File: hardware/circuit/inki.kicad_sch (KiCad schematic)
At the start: 40 parts, among them J1 connector epaper, J2 Conn_01x02_Socket, J3 Conn_01x02_Socket, J4 Conn_01x02_Socket, J5 Conn_01x02_Socket, J7 Conn_01x02_Socket, Q1 TSM260P02CX, Q2 MMBT3904, Q3 IRLML6344TRPBF, SW1 SW_DIP_x04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

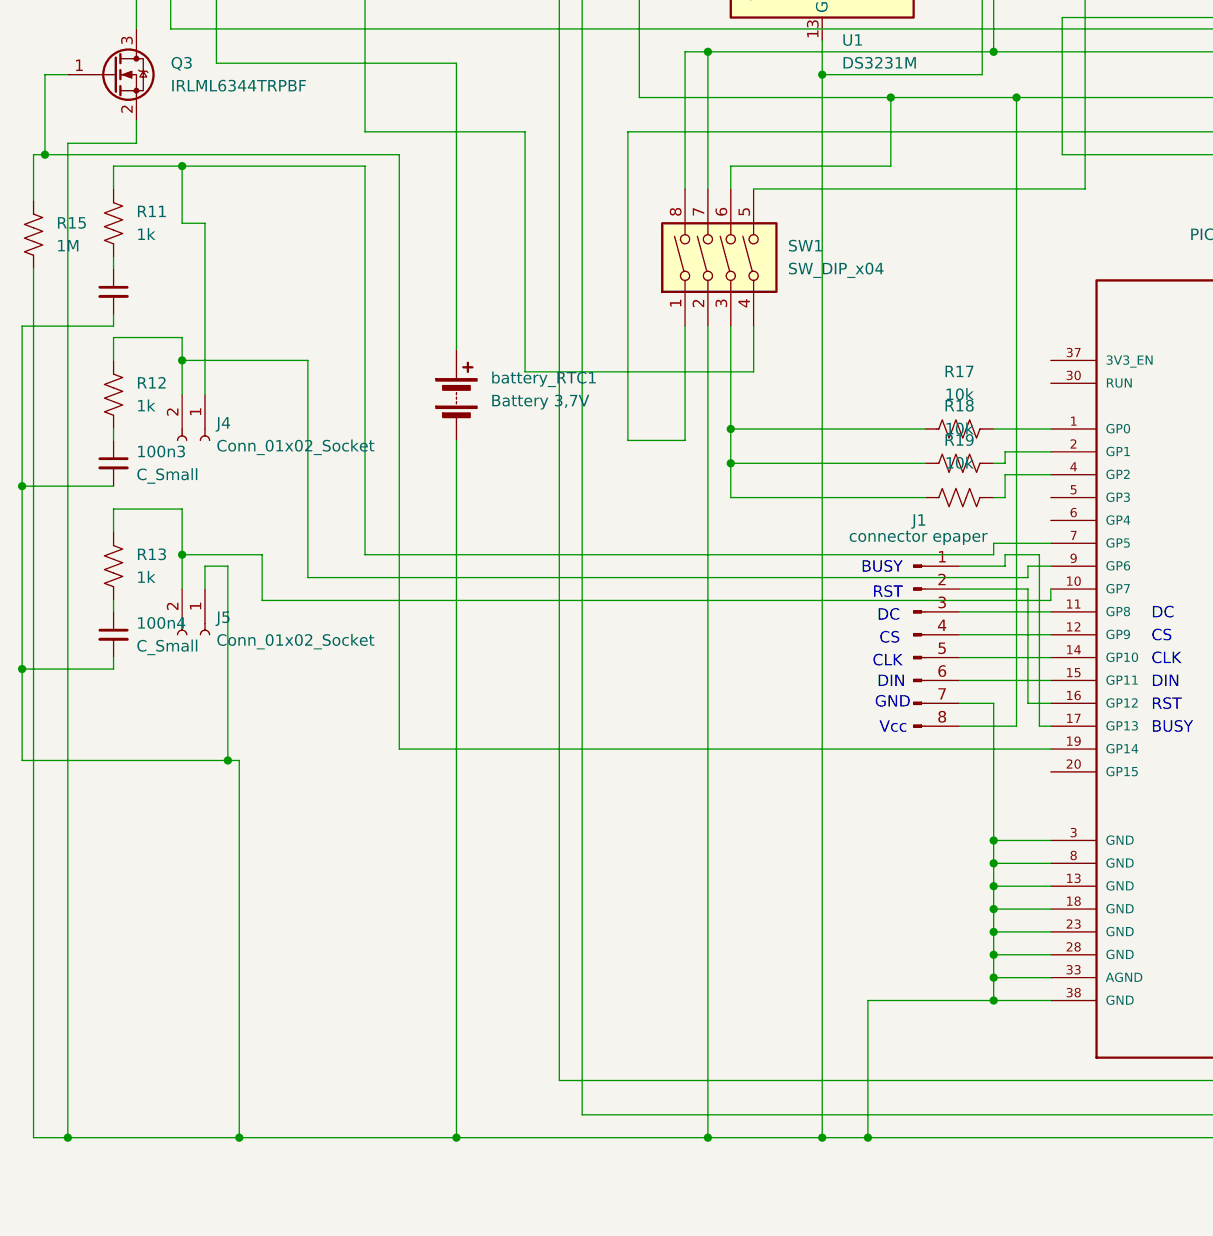
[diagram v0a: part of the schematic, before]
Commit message: modified pcb (all smds to one side), weathermap work
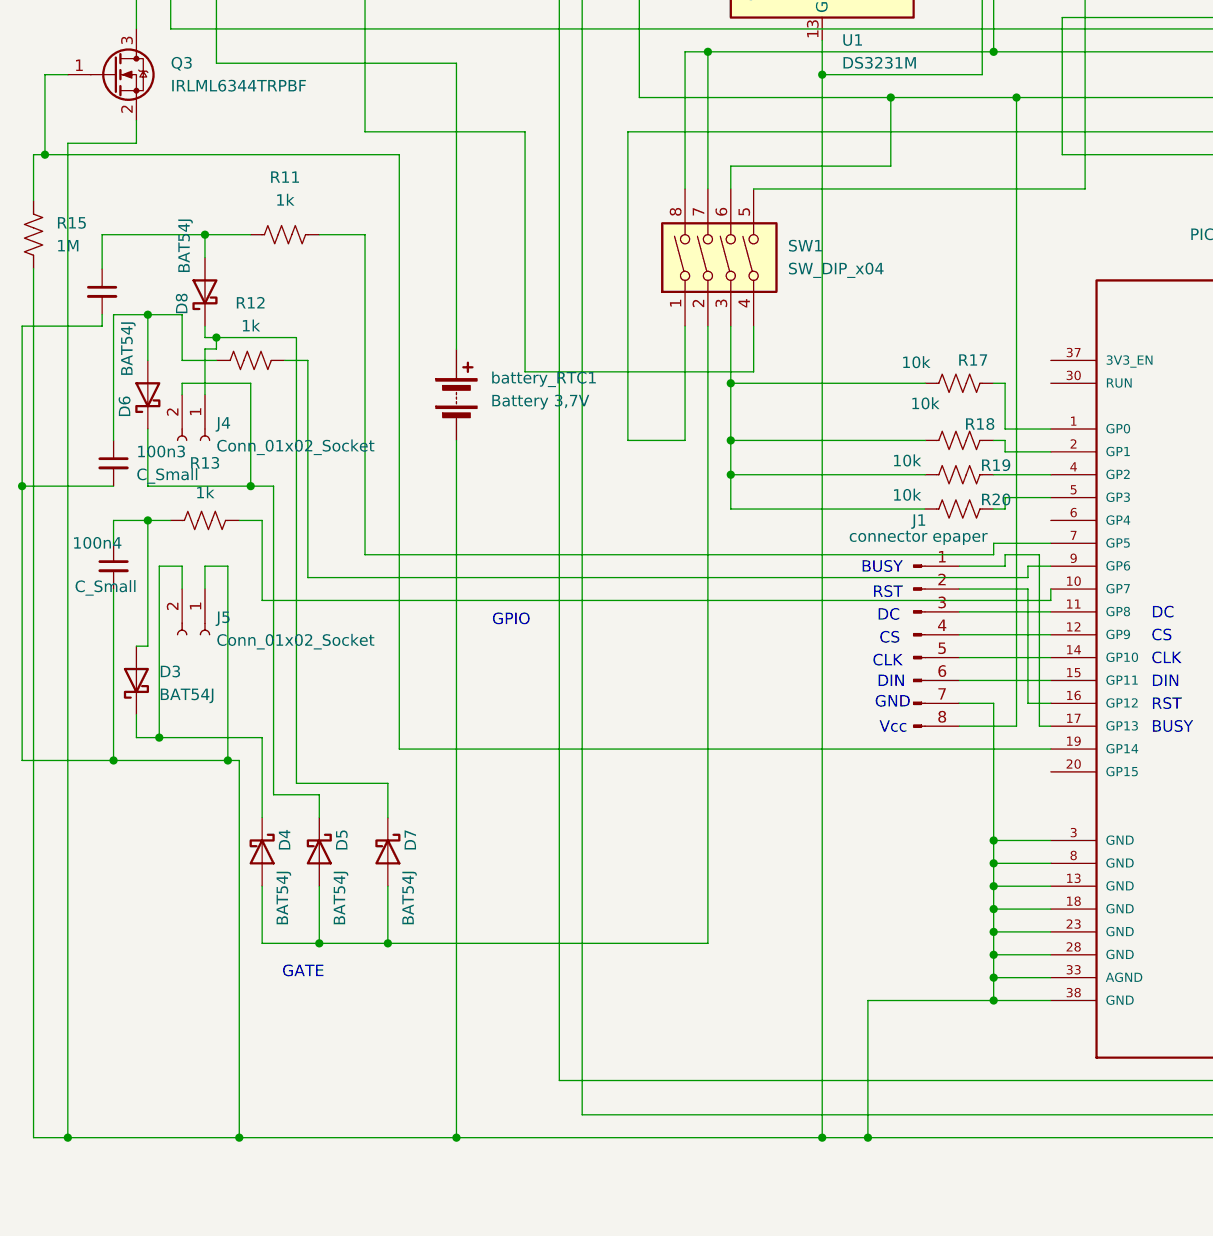
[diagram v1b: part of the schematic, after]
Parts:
- added D3, D4, D5, D6, D7, D8: BAT54J, Diode_SMD:D_SOD-323_HandSoldering, symbol Diode:BAT54J
- added R20: 10k, Resistor_SMD:R_0805_2012Metric_Pad1.20x1.40mm_HandSolder, symbol Device:R_US
- D1: footprint Diode_SMD:D_SOD-323F -> Diode_SMD:D_SOD-323_HandSoldering
- D2: footprint Diode_SMD:D_SOD-323 -> Diode_SMD:D_SOD-323_HandSoldering
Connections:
- net GND: no longer SW1.2
- net at R17.1, R18.1, R19.1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: now also R20.1
- net at R12.1: now also pico1.9 (GP6); no longer 100n3.1
- net at 100n4.1: now also R13.2, D3.2 (A); no longer R13.1
- net at pico1.5 (GP3): now also R20.2
- net at R11.1: now also pico1.7 (GP5); no longer 100n2.1
- new net: D3.1 (K), D4.1 (K), J5.2 (Pin_2)
- new net: D4.2 (A), D5.2 (A), D7.2 (A), SW1.2
- new net: 100n3.1, D6.2 (A), R12.2
- new net: R13.1, pico1.10 (GP7)
- new net: D7.1 (K), D8.1 (K), J4.1 (Pin_1)
- new net: D5.1 (K), D6.1 (K), J4.2 (Pin_2)
- new net: 100n2.1, D8.2 (A), R11.2
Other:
- note added: "GATE"
- note added: "GPIO"
- moved on the sheet: 100n4, R11, R12, R13, R17, R18, R19

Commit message: edit pcb: add bmp581
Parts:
- added U2: BMP581, symbol BMP581:BMP581
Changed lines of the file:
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@@
+	)
+	(symbol
+		(lib_id "BMP581:BMP581")
+		(at 250.19 148.59 0)
+		(unit 1)
+		(exclude_from_sim no)
+		(in_bom yes)
+		(on_board yes)
+		(dnp no)
+		(fields_autoplaced yes)
+		(property "Reference" "U2"
+			(at 250.825 138.43 0)
+			(effects
+				(font
+					(size 1.27 1.27)
+				)
+			)
+		)
+		(property "Value" "BMP581"
+			(at 250.825 140.97 0)
+			(effects
+				(font
+					(size 1.27 1.27)
+				)
+			)
+		)
+		(property "Footprint" ""
+			(at 250.19 148.59 0)
+			(effects
+				(font
+					(size 1.27 1.27)
+				)
+				(hide yes)
+			)
+		)
+		(property "Datasheet" ""
+			(at 250.19 148.59 0)
+			(effects
+				(font
+					(size 1.27 1.27)
+				)
+				(hide yes)
+			)
+		)
+		(property "Description" ""
+			(at 250.19 148.59 0)
+			(effects
+				(font
+					(size 1.27 1.27)
+				)
+				(hide yes)
+			)
+		)
+		(pin "8"
+		)
+		(pin "7"
+		)
+		(pin "4"
+		)
+		(pin "3"
+		)
+		(pin "1"
+		)
+		(pin "2"
+		)
+		(pin "6"
+		)
+		(pin "5"
+		)
+		(pin "10"
+		)
+		(pin "9"
+		)
+		(instances
+			(project ""
+				(path "/240a819b-80d5-474c-958b-cef4297f8f8c"
+					(reference "U2")
+					(unit 1)
+				)
+			)
+		)
 	)
 	(symbol

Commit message: default config weathermap
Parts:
- added 100n5: C_Small, Capacitor_SMD:C_0805_2012Metric, symbol Device:C_Small
- U2: footprint (none) -> inki:BMP581
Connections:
- net GND: now also U2.3 (VSS), U2.7 (INT), U2.8 (VSS), U2.9 (VSS), 100n5.2
- net at R3.2, U1.15 (SDA), pico1.26 (GP20): now also U2.4 (SDI)
- net at R4.2, U1.16 (SCL), pico1.27 (GP21): now also U2.2 (SCK)
- net at C1.1, C3.1, J1.8 (Pin_8)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: now also U2.1 (VDDIO), U2.10 (VDD), U2.5 (SDO), U2.6 (CSB), 100n5.1

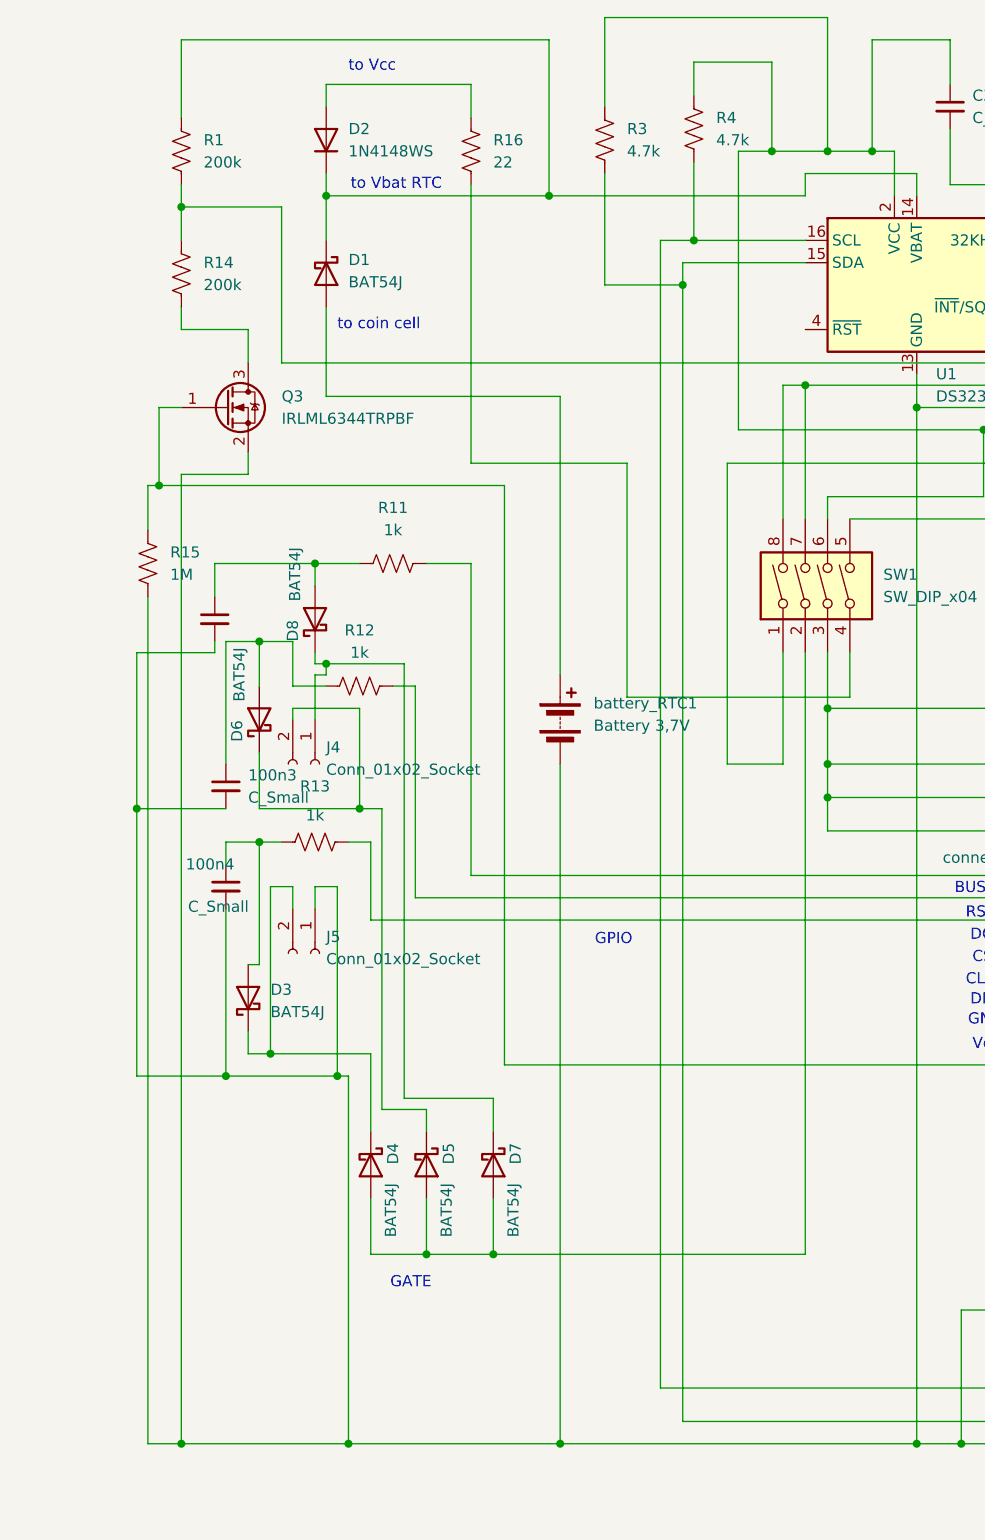
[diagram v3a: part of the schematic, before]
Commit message: hardware: gate VBAT divider with PFET to stop leakage in off-state
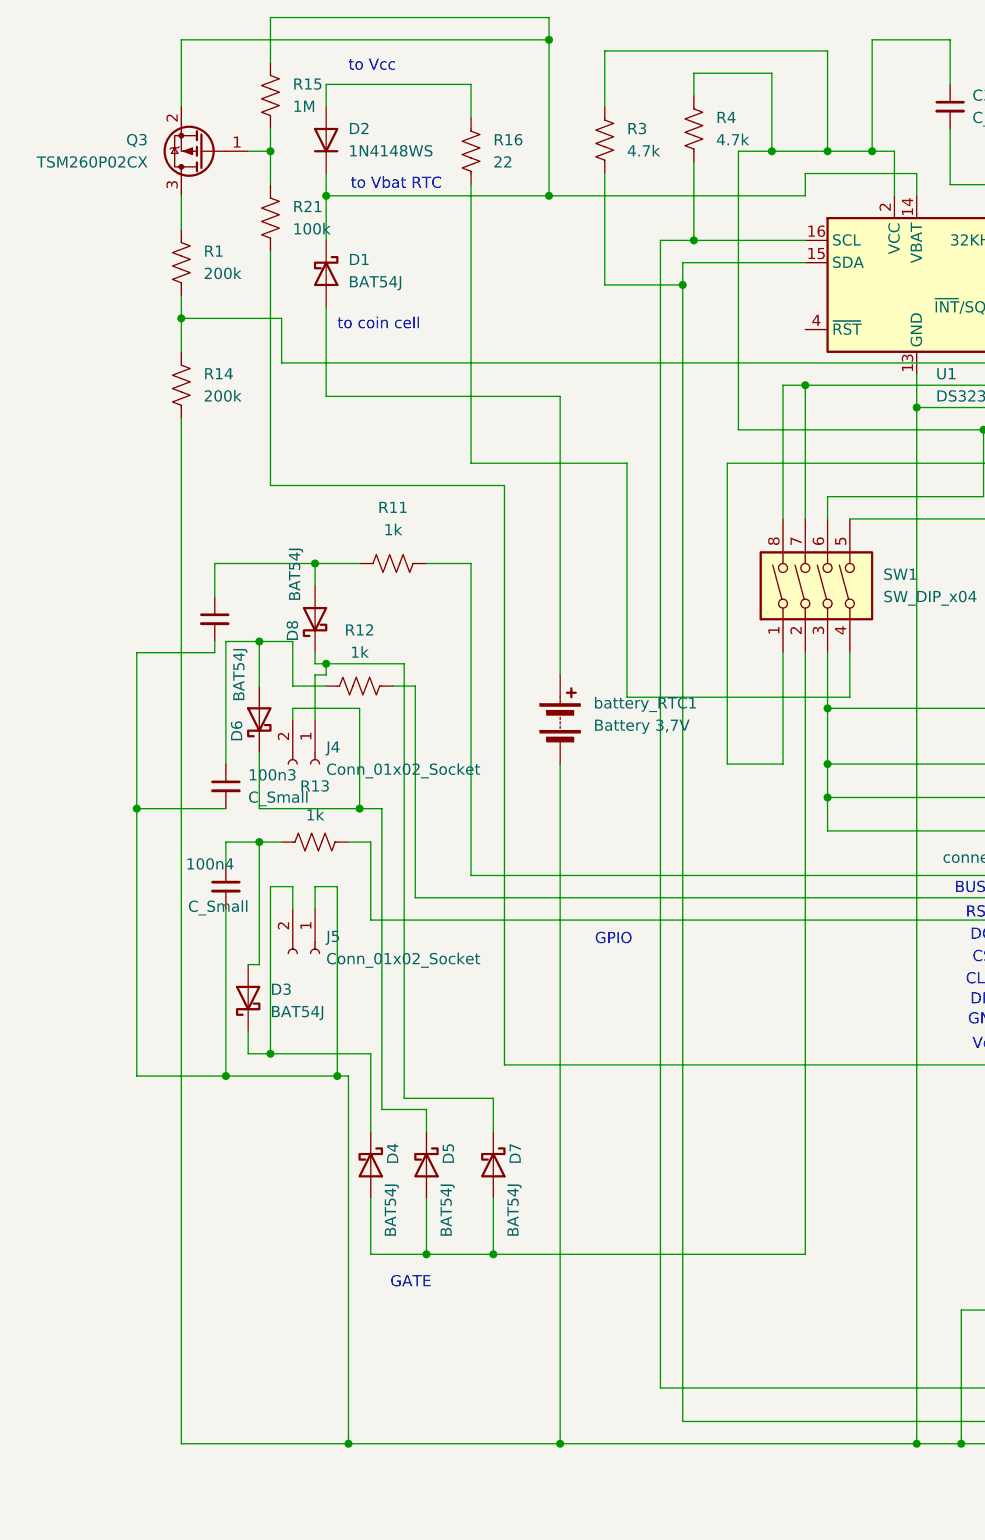
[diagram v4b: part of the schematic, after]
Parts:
- removed Q3: IRLML6344TRPBF, Package_TO_SOT_SMD:SOT-23, symbol Transistor_FET:IRLML0030
- added Q3: TSM260P02CX, Package_TO_SOT_SMD:SOT-23_Handsoldering, symbol Transistor_FET:TSM2301ACX
- added R21: 100k, Resistor_SMD:R_0805_2012Metric_Pad1.20x1.40mm_HandSolder, symbol Device:R_US
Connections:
- net GND: now also R14.2; no longer R15.2
- net at D1.1 (K), D2.1 (K), U1.14 (VBAT): now also R15.1, Q3.2 (S); no longer R1.1
- net at pico1.19 (GP14): now also R21.2; no longer R15.1
- new net: Q3.1 (G), R15.2, R21.1
- new net: Q3.3 (D), R1.1
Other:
- moved on the sheet: R1, R14

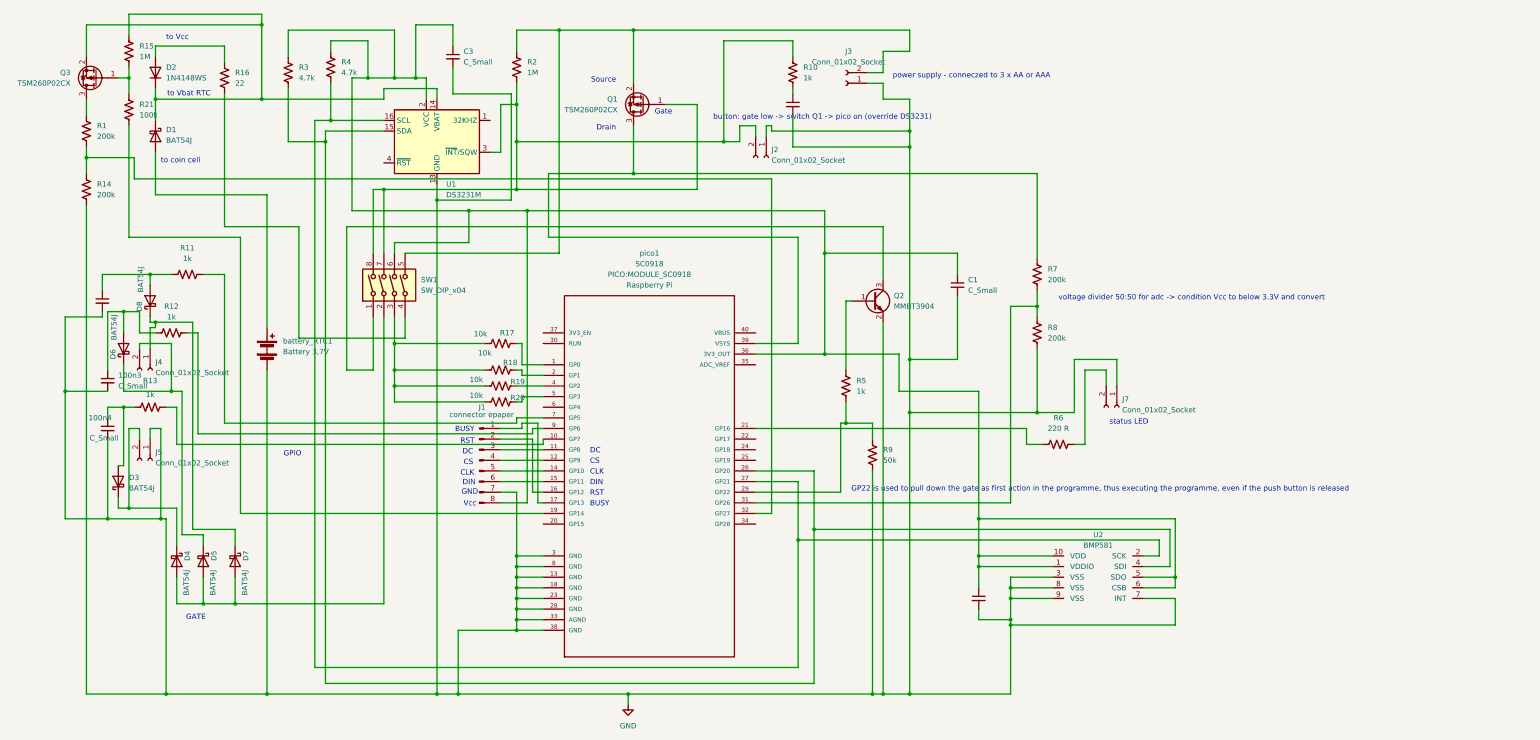
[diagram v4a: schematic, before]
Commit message: improved coin cell voltage measurement
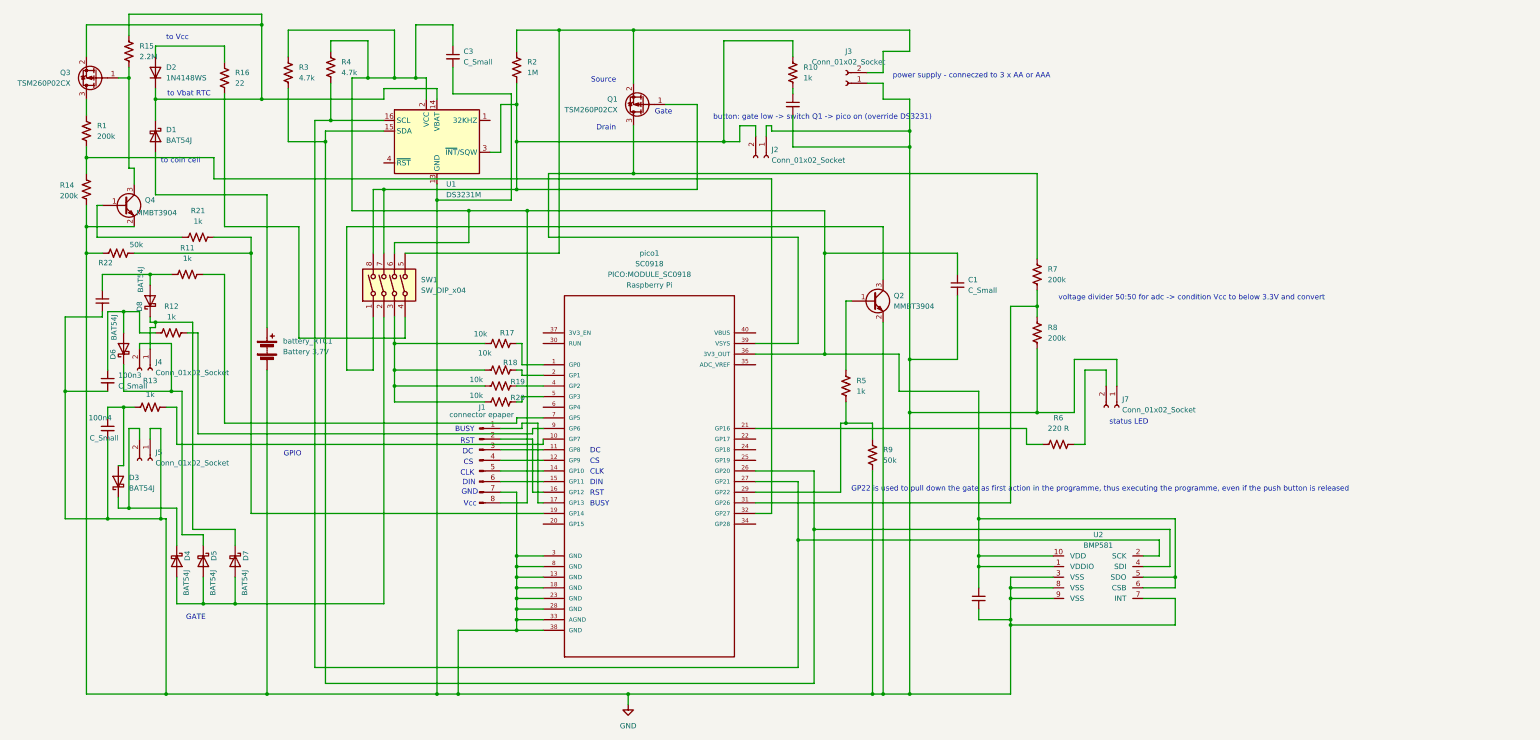
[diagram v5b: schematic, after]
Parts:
- added Q4: MMBT3904, Package_TO_SOT_SMD:SOT-23, symbol Transistor_BJT:MMBT3904
- added R22: 50k, Resistor_SMD:R_0805_2012Metric_Pad1.20x1.40mm_HandSolder, symbol Device:R_US
- R15: value 1M -> 2.2M
- R21: value 100k -> 1k
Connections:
- net GND: now also Q4.2 (E), R22.1
- net at Q3.1 (G), R15.2: now also Q4.3 (C); no longer R21.1
- net at pico1.19 (GP14): now also R21.1, R22.2; no longer R21.2
- new net: Q4.1 (B), R21.2
